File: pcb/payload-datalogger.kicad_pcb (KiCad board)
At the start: 2 copper layers, 56 x 43 mm, 55 parts, among them J1 2.54mm 01x02 header, J2 DE15 Socket, J3 Conn_01x04_Pin, J4 Conn_01x02_Pin, SW2 PTS815, SW3 PTS815, U2 BU33SD5, U3 W25X40CLSN, U4 MCP96RL00T-E_MX, U5 MCP96RL00T-E_MX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

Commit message: Rearrange battery and LDO
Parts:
- moved C3 12.0 mm to (89.9, 72.0), turned to 0 degrees
- moved BT1 9.49 mm to (100.0, 74.5), turned to -90 degrees
- moved U2 9.30 mm to (89.7, 75.2), turned to -90 degrees
- moved C1 7.74 mm to (94.2, 67.0), turned to 180 degrees
- moved C2 7.68 mm to (89.9, 78.5), turned to 180 degrees
- moved J1 7.44 mm to (94.0, 74.0), turned to 0 degrees
- moved R4 4.96 mm to (94.2, 69.0), turned to 180 degrees
- moved R6 4.00 mm to (83.7, 77.5), turned to 0 degrees
- moved SW2 2.61 mm to (93.2, 63.9), turned to 0 degrees
- moved R3 2.28 mm to (94.2, 71.0), turned to 0 degrees
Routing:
- net +3V3: track 17.8 -> 24.5 mm, vias 6 -> 7
- net /BATT_MEAS: track 22.9 -> 20.4 mm
- net Net-(BT1--): track 5.00 -> 6.00 mm
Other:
- board text added: "BATT"
- board text removed: "BATTERY"

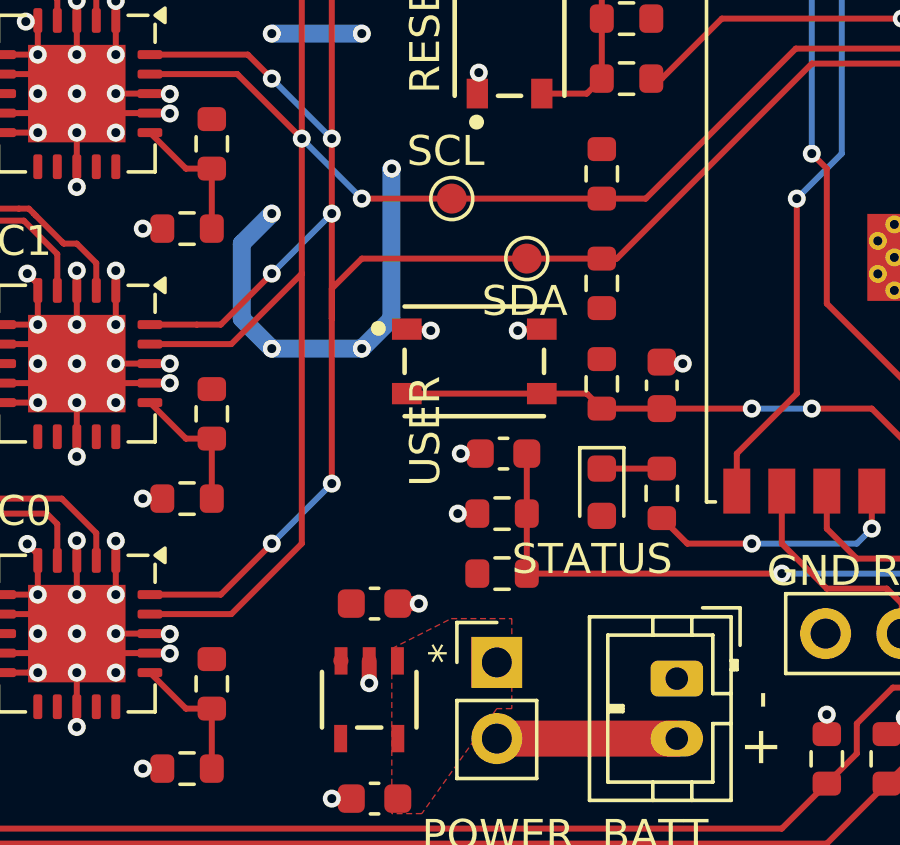
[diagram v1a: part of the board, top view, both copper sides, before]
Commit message: Fix silkscreen overlap in DRC
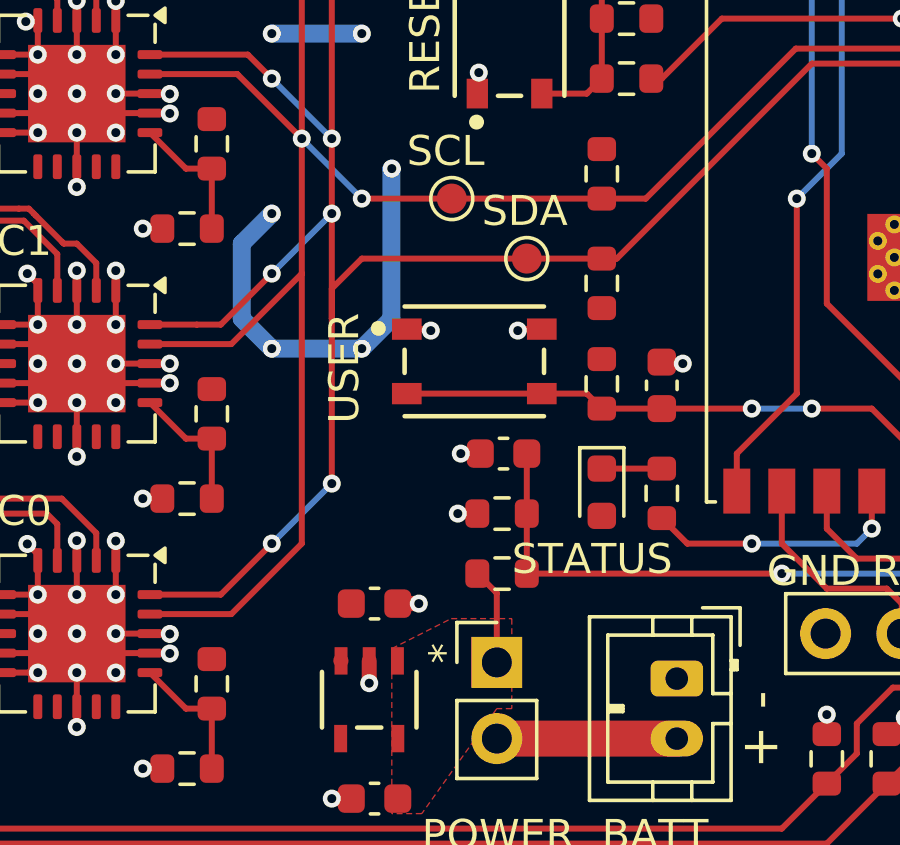
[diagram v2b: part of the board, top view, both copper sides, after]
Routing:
- net +BATT: track 0.00 -> 3.23 mm
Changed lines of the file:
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@@
 	)
 	(gr_text "SDA"
-		(at 93.5 62.5 0)
+		(at 93.5 59.5 0)
 		(layer "F.SilkS")
 		(effects
@@
 	)
 	(gr_text "USER"
-		(at 92.2 68.1 90)
+		(at 89.5 66 90)
 		(layer "F.SilkS")
 		(effects
@@
 	)
 	(segment
+		(start 94 73.96)
+		(end 94 71.65)
+		(width 0.2)
+		(layer "F.Cu")
+		(net 5)
+	)
+	(segment
+		(start 94 71.65)
+		(end 93.35 71)
+		(width 0.2)
+		(layer "F.Cu")
+		(net 5)
+	)
+	(segment
